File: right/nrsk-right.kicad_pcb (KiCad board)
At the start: 2 copper layers, 187 x 120.3 mm, 127 parts, among them J1 PJ-320D, J2 USB-C, SW1 71, SW10 8, SW11 9, SW12 0, SW13 -, SW14 =, SW15 Backspace, SW16 75, SW17 Y, SW18 U, SW19 I, SW2 F7, SW20 O, SW21 P, SW22 [, SW23 ], SW24 \, SW25 77, SW26 H, SW27 J, SW28 K, SW29 L, SW3 F8, SW30 ;, SW31 ', SW32 Enter, SW33 79, SW34 N, SW35 M, SW36 ,, SW37 ., SW38 /, SW39 ↑, SW4 F9, SW40 fn, SW41 81, SW42 Space, SW43 Space, SW44 Cmd, SW45 Opt, SW46 ←, SW47 ↓, SW48 →, SW5 F10, SW6 F11, SW7 F12, SW8 73, SW9 7, U1 ATmega32U4-AU, U2 USBLC6-2SC6, Y1 16MHz

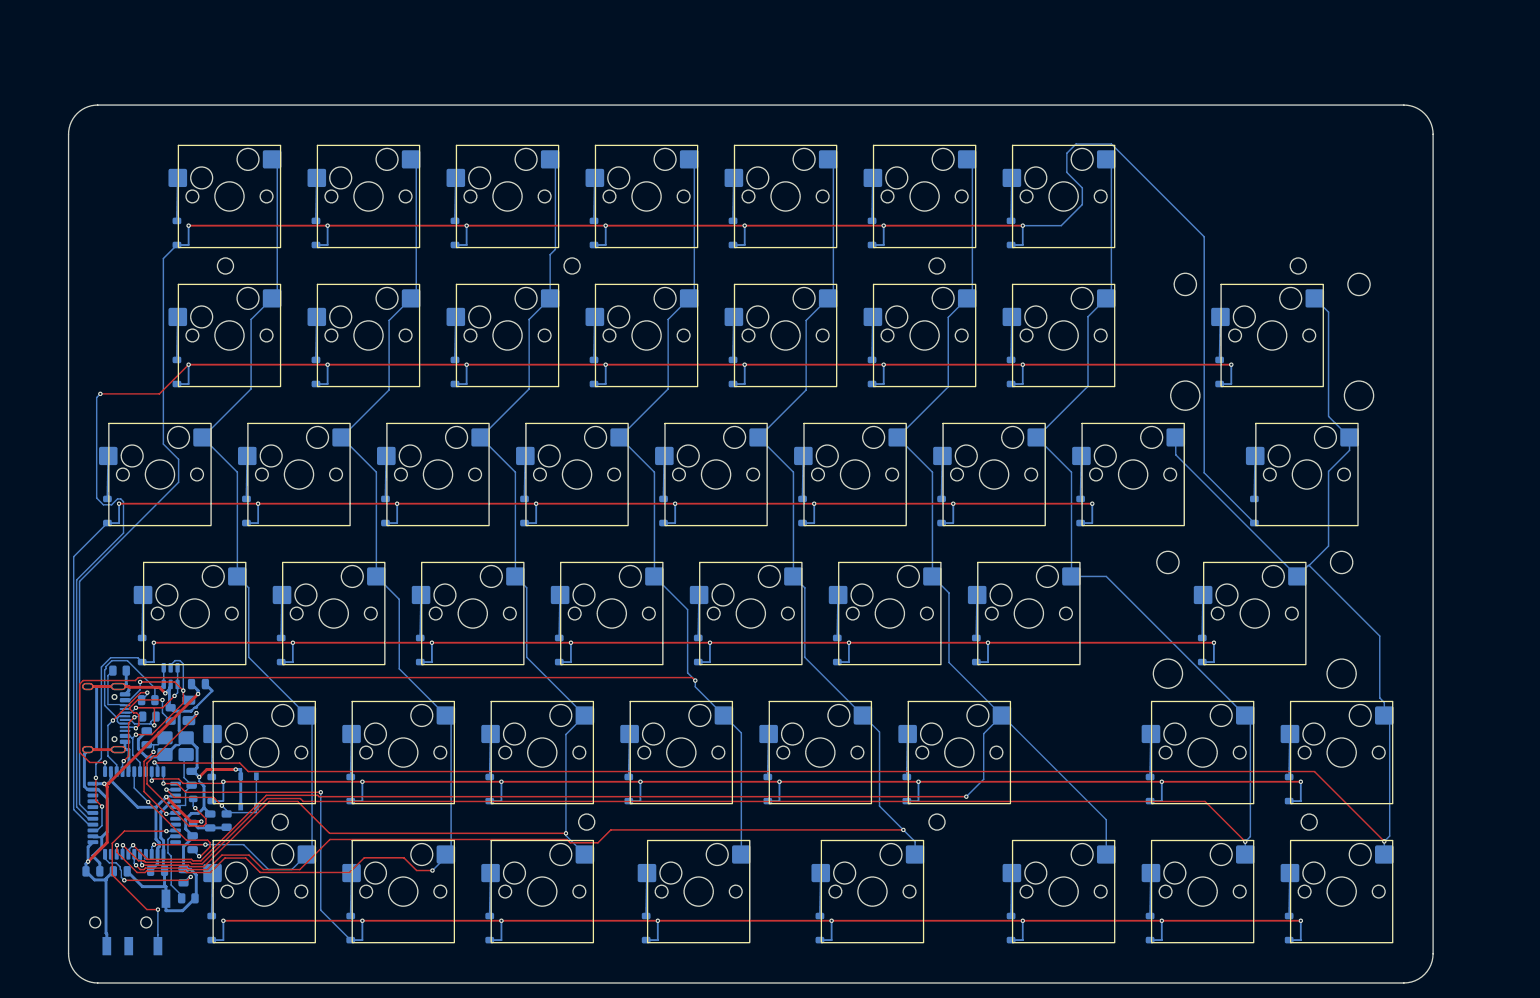
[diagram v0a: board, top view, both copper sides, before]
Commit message: Add OLED displays, OLED placement study and high-resolution renders
- 0.91" 128x32 SSD1306 OLED on both halves (I2C on PD0/PD1, 4.7k pull-ups),
  placed in the key-free inner notch; boards re-routed, ERC/DRC clean
- Switch plate window with a 2 mm clear acrylic cover lying on the plate,
  shaped around the switch tops; keyboard height unchanged
- QMK: OLED enabled (layer/caps on the master, WPM on the other half),
  split sync of layer, LED state and WPM
- BOM: OLED modules, pull-ups, cover acrylic and screws
- OLED height/tilt study: flush, 3.5/6.5/13 mm pods and two tilted pods,
  checked clear of keycaps and inside the case outline
- Blender renders at 2400 px and a grouped, numbered overview sheet

Co-Authored-By: Claude Opus 5.5 <noreply@anthropic.com>
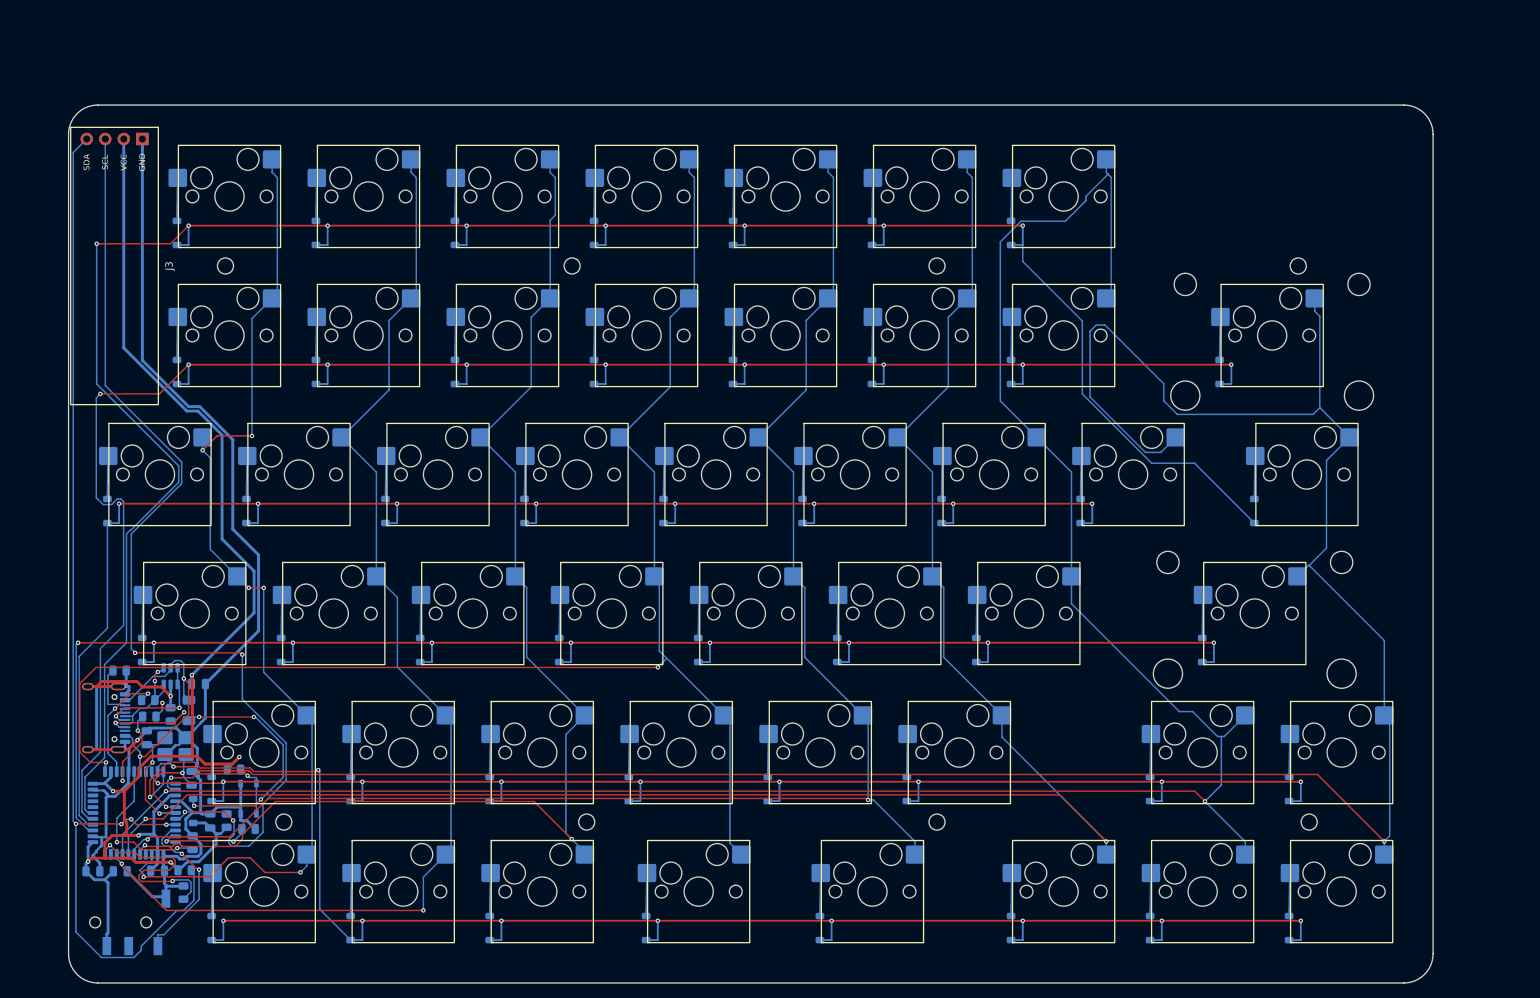
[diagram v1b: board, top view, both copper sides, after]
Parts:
- added J3: OLED 128x32, nrsk:OLED_0.91in_128x32_I2C, F.Cu at (33.3, 49.0)
- added R8: 4.7k, Resistor_SMD:R_0805_2012Metric, B.Cu at (48.7, 125.0)
- added R9: 4.7k, Resistor_SMD:R_0805_2012Metric, B.Cu at (42.9, 131.8)
- moved R1 12.6 mm to (51.7, 126.2)
- moved R6 7.07 mm to (49.7, 118.0), turned to 0 degrees
- moved R7 2.25 mm to (42.8, 134.9)
- moved RSW1 1.00 mm to (51.7, 122.0)
- moved H5 0.50 mm to (56.5, 125.2)
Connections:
- U1 pad 18: unconnected-(U1-PD0-Pad18) -> /SCL
- U1 pad 19: unconnected-(U1-PD1-Pad19) -> /SDA
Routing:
- net /SDA: track 0.00 -> 149.3 mm, vias 0 -> 4
- net /SCL: track 0.00 -> 140.0 mm, vias 0 -> 4
- net VCC: track 86.5 -> 199.6 mm, vias 5 -> 6
- net GND: track 153.8 -> 232.3 mm, vias 3 -> 2
- net /COL7: track 288.0 -> 324.3 mm
- net /COL6: track 277.2 -> 298.2 mm
- net /ROW0: track 314.2 -> 301.2 mm, vias 7 -> 8
- net /HWB: track 15.8 -> 28.1 mm
- net /COL0: track 130.9 -> 142.6 mm, vias 2 -> 6
- net /ROW5: track 227.3 -> 238.0 mm
- net /USB_D-: track 24.6 -> 14.7 mm, vias 0 -> 2
- net /COL5: track 245.1 -> 253.1 mm
- net /ROW3: track 209.5 -> 216.8 mm, vias 10 -> 9
- net /COL4: track 220.1 -> 213.3 mm
- net /XTAL2: track 9.33 -> 15.0 mm, vias 0 -> 2
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
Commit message: Match both halves' size, align TRRS jacks, document firmware flashing
- Left board widened on its inner side to the right board's outline
  (both 187.0 x 120.3 mm, cases 204.0 x 137.3 mm); MCU, USB-C, TRRS and
  OLED placed as a mirror of the right half
- TRRS jacks at the same height on both halves (109 mm from the top),
  USB-C likewise (81 mm)
- Router cleanup removes dangling track stubs left by Freerouting
- README: step-by-step QMK build and DFU flashing for each half,
  troubleshooting and ISP recovery
- Renders and OLED study regenerated for the new layout

Co-Authored-By: Claude Opus 5.5 <noreply@anthropic.com>
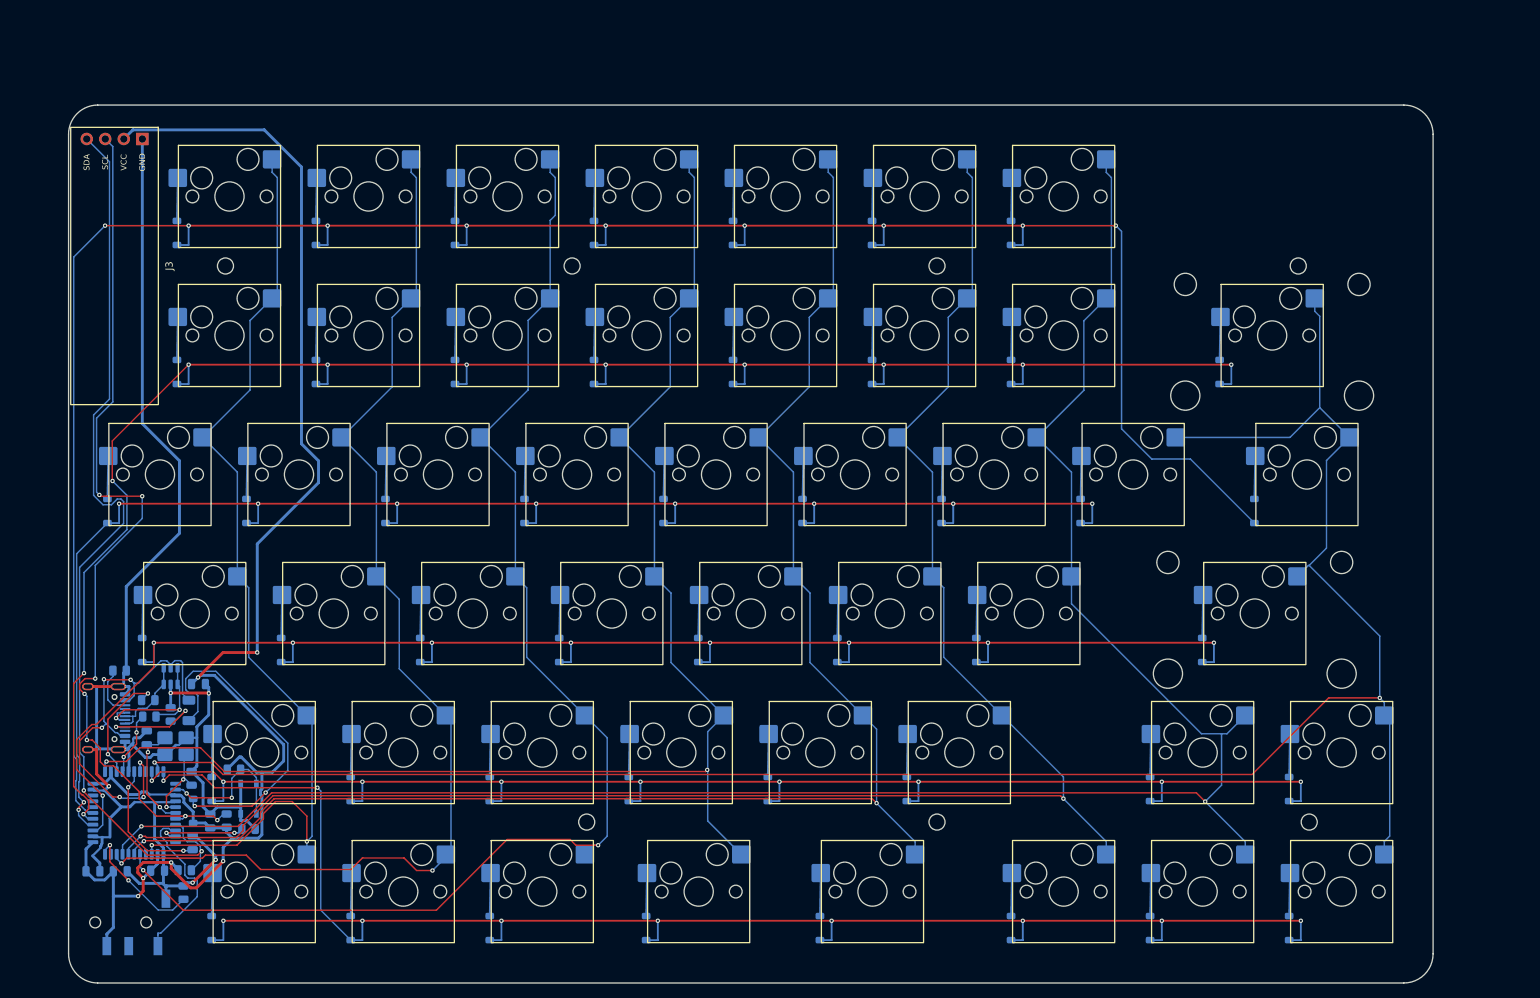
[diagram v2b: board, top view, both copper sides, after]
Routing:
- net /COL7: track 324.3 -> 283.3 mm
- net VCC: track 199.6 -> 227.7 mm
- net /COL6: track 298.2 -> 272.4 mm
- net /SDA: track 149.3 -> 128.0 mm, vias 4 -> 2
- net /VBUS: track 36.5 -> 56.2 mm, vias 2 -> 6
- net /SCL: track 140.0 -> 121.7 mm, vias 4 -> 7
- net /VFUSE: track 34.0 -> 45.5 mm, vias 4 -> 2
- net /HWB: track 28.1 -> 17.2 mm
- net /ROW5: track 238.0 -> 227.8 mm
- net /COL3: track 203.4 -> 194.6 mm
- net /COL5: track 253.1 -> 244.2 mm
- net /ROW1: track 256.4 -> 249.4 mm, vias 9 -> 11
- net /COL0: track 142.6 -> 136.0 mm, vias 6 -> 2
- net /COL2: track 173.3 -> 179.8 mm
- net /COL1: track 160.9 -> 156.0 mm
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
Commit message: Add corner thumbwheels read by AS5600, preview-quality renders
- Thumbwheel (29.2 mm, knurled) at the left half's top-left and the right
  half's top-right corner, lying under the PCB with its rim out of the
  corner; read contact-free by an AS5600 on the PCB back through a
  diametric magnet, on the existing I2C bus (no extra pins)
- Left Esc switch turned 180 deg so its socket clears the sensor
- Case: wall opening at the corner, axle post (print) / M3 axle (acrylic),
  corner screws moved beside the opening, printable wheel STL
- QMK: nrsk.c polls the sensor and forwards the other half's steps over a
  split RPC; dial_update_user() in the keymap (volume / page by default)
- Router cleanup runs in a separate process (reloading a board in the
  same process returned a broken object and stopped the build)
- Renders default to a quick preview (1200 px); FINAL=1 for 2400 px
- Side dial comparison renders kept in docs/img/dial-study

Co-Authored-By: Claude Opus 5.5 <noreply@anthropic.com>
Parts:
- added C10: 0.1uF, Capacitor_SMD:C_0805_2012Metric, B.Cu at (206.5, 35.9)
- added C9: 1uF, Capacitor_SMD:C_0805_2012Metric, B.Cu at (204.0, 32.6)
- added U3: AS5600-ASOM, Package_SO:SOIC-8_3.9x4.9mm_P1.27mm, B.Cu at (209.0, 32.0)
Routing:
- net GND: track 229.1 -> 423.6 mm, vias 5 -> 6
- net /SCL: track 121.7 -> 302.1 mm, vias 7 -> 5
- net /SDA: track 128.0 -> 298.2 mm, vias 2 -> 4
- net VCC: track 227.7 -> 371.0 mm, vias 6 -> 7
- net /ROW0: track 303.8 -> 364.5 mm
- net /DATA: track 23.2 -> 50.5 mm, vias 0 -> 2
- net /VFUSE: track 45.5 -> 22.7 mm
- net /XTAL1: track 14.7 -> 31.3 mm
- net /VBUS: track 56.2 -> 43.3 mm, vias 6 -> 4
- net /ROW2: track 212.4 -> 224.6 mm, vias 10 -> 11
- net /HWB: track 17.2 -> 28.1 mm, vias 2 -> 0
- net /COL2: track 179.8 -> 170.0 mm
- net /D+: track 8.69 -> 17.5 mm
- net /CC1: track 14.3 -> 9.10 mm
- net /ROW5: track 227.8 -> 223.1 mm
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
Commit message: Fit boards and cases tightly, align TRRS, add sourced BOM
- Board/case outlines shrink to each half's key area (left 163.2 mm,
  right 187.0 mm wide); TRRS jacks at the same height on both halves
- build.sh: per-step failure handling in the routing loop
- gen/doc_images.sh regenerates the README board/case images
- BOM: manufacturer part numbers, shops, prices and verified URLs
  from gen/bom_sources.json; README notes parts to check before ordering

Co-Authored-By: Claude Opus 5.5 <noreply@anthropic.com>
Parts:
- moved R1 11.7 mm to (42.9, 133.9)
- moved R7 10.8 mm to (32.0, 134.2), turned to 0 degrees
- moved J1 3.30 mm to (35.4, 142.3)
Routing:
- net /ROW0: track 364.5 -> 323.2 mm, vias 9 -> 8
- net /DATA: track 50.5 -> 24.7 mm
- net /HWB: track 28.1 -> 4.97 mm
- net /XTAL1: track 31.3 -> 14.9 mm
- net /SCL: track 302.1 -> 290.7 mm, vias 5 -> 3
- net /COL5: track 242.4 -> 253.6 mm
- net GND: track 423.6 -> 434.5 mm, vias 6 -> 4
- net /ROW2: track 224.6 -> 214.3 mm, vias 11 -> 10
- net /COL7: track 282.0 -> 291.9 mm
- net /VBUS: track 43.3 -> 36.4 mm, vias 4 -> 5
- net /SDA: track 298.2 -> 303.5 mm
- net /D+: track 17.5 -> 22.8 mm
- net /COL3: track 192.7 -> 197.7 mm
- net /ROW1: track 251.8 -> 254.7 mm, vias 9 -> 11
- net /ROW4: track 193.2 -> 196.0 mm, vias 9 -> 10
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
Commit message: Align OLEDs, show KiCad-assembled boards in the viewer, add explode gap slider
- Left OLED moves to the top two rows like the right one; the left board
  grows 4.7 mm on the inner edge to keep the same switch clearance
- Footprints carry 3D models: kiswitch MX switch / Kailh socket /
  stabilizer, LCSC USB-C and PJ-320D (fetched by gen/fetch_3d.sh into
  tools/), and a simple OLED module model (gen/models3d.py)
- gen/export_3d.py exports each board as GLB; gen/glb_mesh.py merges,
  dedupes and quantises it into instanced meshes for case/preview/viewer.html
- Viewer: exploded view gets a layer-gap slider (0-40 mm)
- BOM/README: both LCSC TRRS jacks verified against the KiCad pad layout

Co-Authored-By: Claude Opus 5.5 <noreply@anthropic.com>
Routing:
- net /ROW2: track 214.3 -> 250.7 mm, vias 10 -> 9
- net /ROW0: track 323.2 -> 294.1 mm, vias 8 -> 11
- net /COL7: track 291.9 -> 320.7 mm
- net /SCL: track 290.7 -> 318.9 mm, vias 3 -> 5
- net GND: track 434.5 -> 411.5 mm, vias 4 -> 6
- net /SDA: track 303.5 -> 319.8 mm
- net /ROW5: track 222.0 -> 207.4 mm, vias 10 -> 9
- net /COL2: track 169.1 -> 181.4 mm
- net /VFUSE: track 24.2 -> 12.2 mm, vias 4 -> 0
- net /USB_D-: track 13.1 -> 23.1 mm
- net /COL0: track 133.2 -> 143.0 mm
- net /USB_D+: track 23.3 -> 17.9 mm, vias 2 -> 3
- net /ROW3: track 214.3 -> 209.0 mm, vias 9 -> 10
- net /COL5: track 253.6 -> 248.4 mm
- net /D+: track 22.8 -> 18.0 mm
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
